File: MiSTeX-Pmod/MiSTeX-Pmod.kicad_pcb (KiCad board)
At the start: 4 copper layers, 64.2 x 51.3 mm, 30 parts, among them CN1 NASB0-S6701-TS50, CN2 NASB0-S6701-TS50, J1 Pmod, J2 USB_A, J3 Conn_01x03_Male, J4 Pmod, J5 Connector_USB_C_Receptacle_US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, SW1 TS-1187A-B-A-B

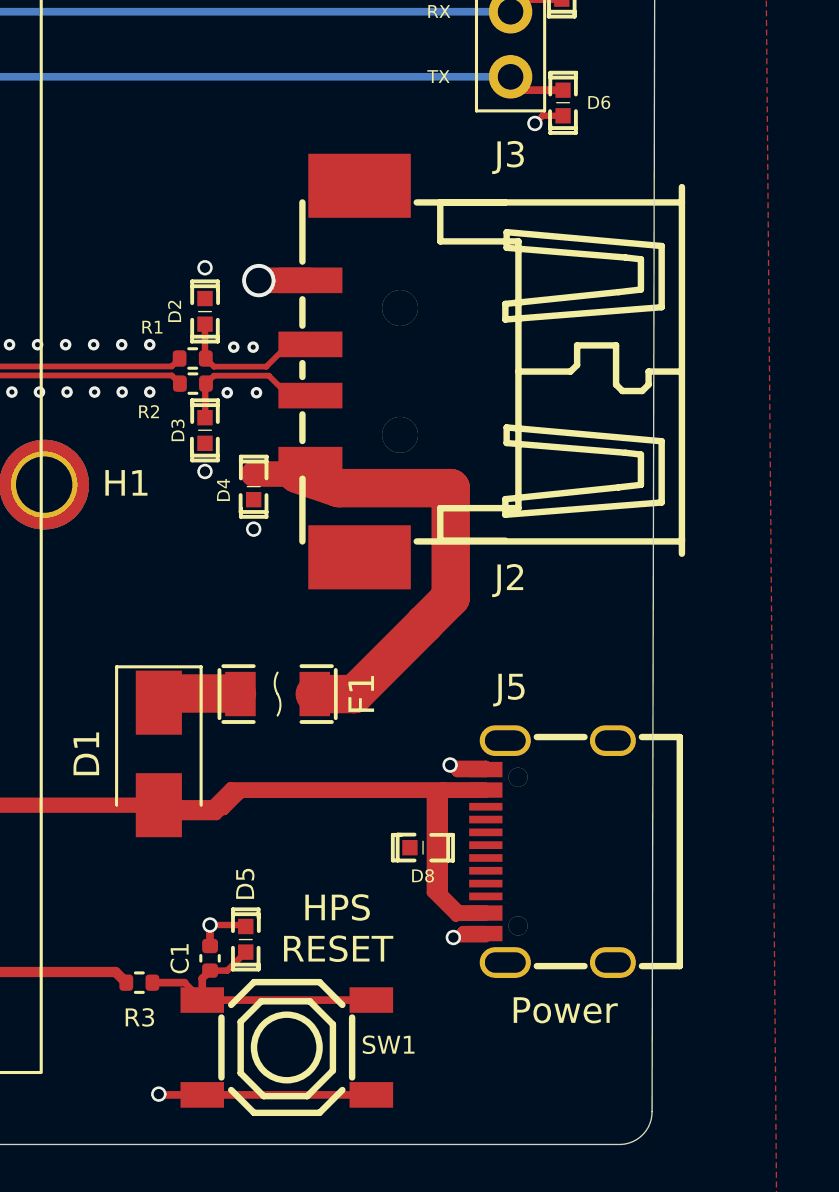
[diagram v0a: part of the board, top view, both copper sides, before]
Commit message: change USB host connector, old one was out of stock
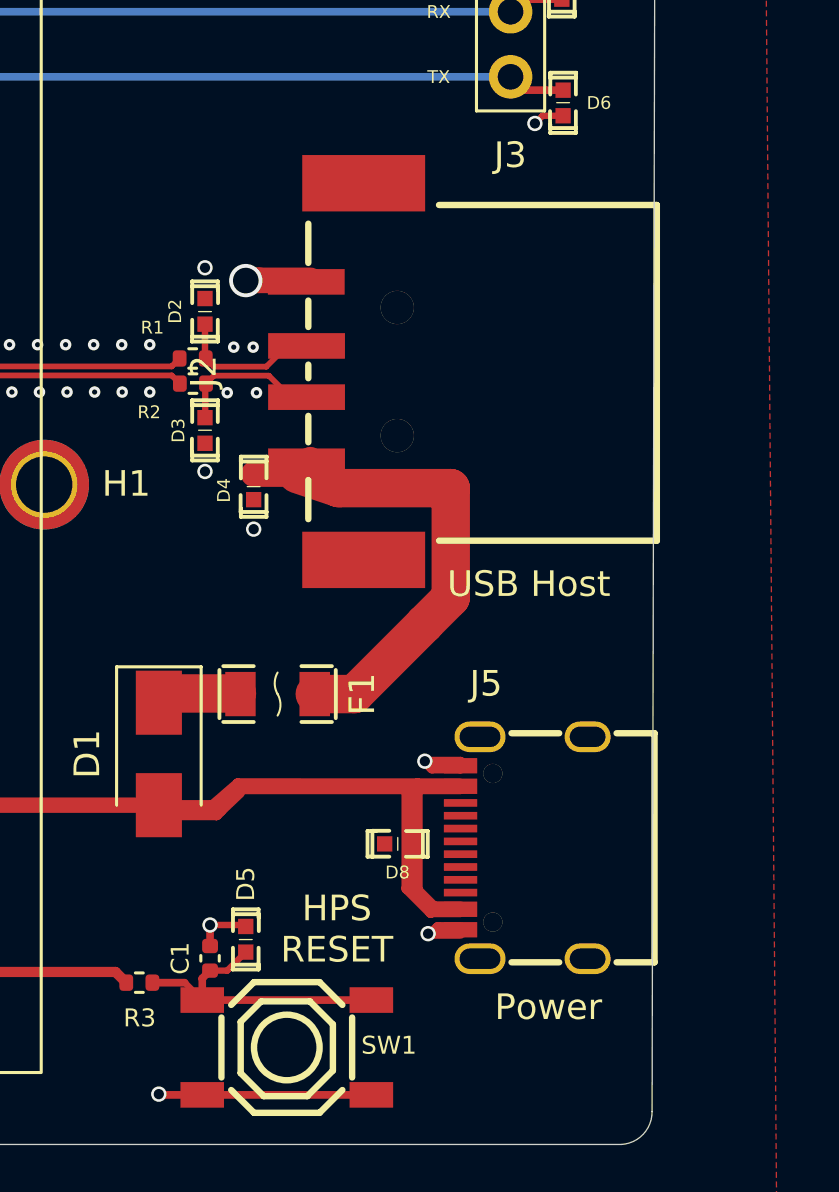
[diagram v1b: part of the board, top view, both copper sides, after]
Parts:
- J2: footprint easyeda2kicad:USB-A-SMD_USB-302S -> easyeda2kicad:USB-A-SMD_GT-USB-2004-CWG1A
- moved D8 1.00 mm to (168.6, 110.3)
- moved J5 1.00 mm to (173.5, 110.5)
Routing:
- net +5V: track 75.7 -> 73.8 mm
- net GND: track 71.4 -> 71.9 mm
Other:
- board text added: "USB Host"

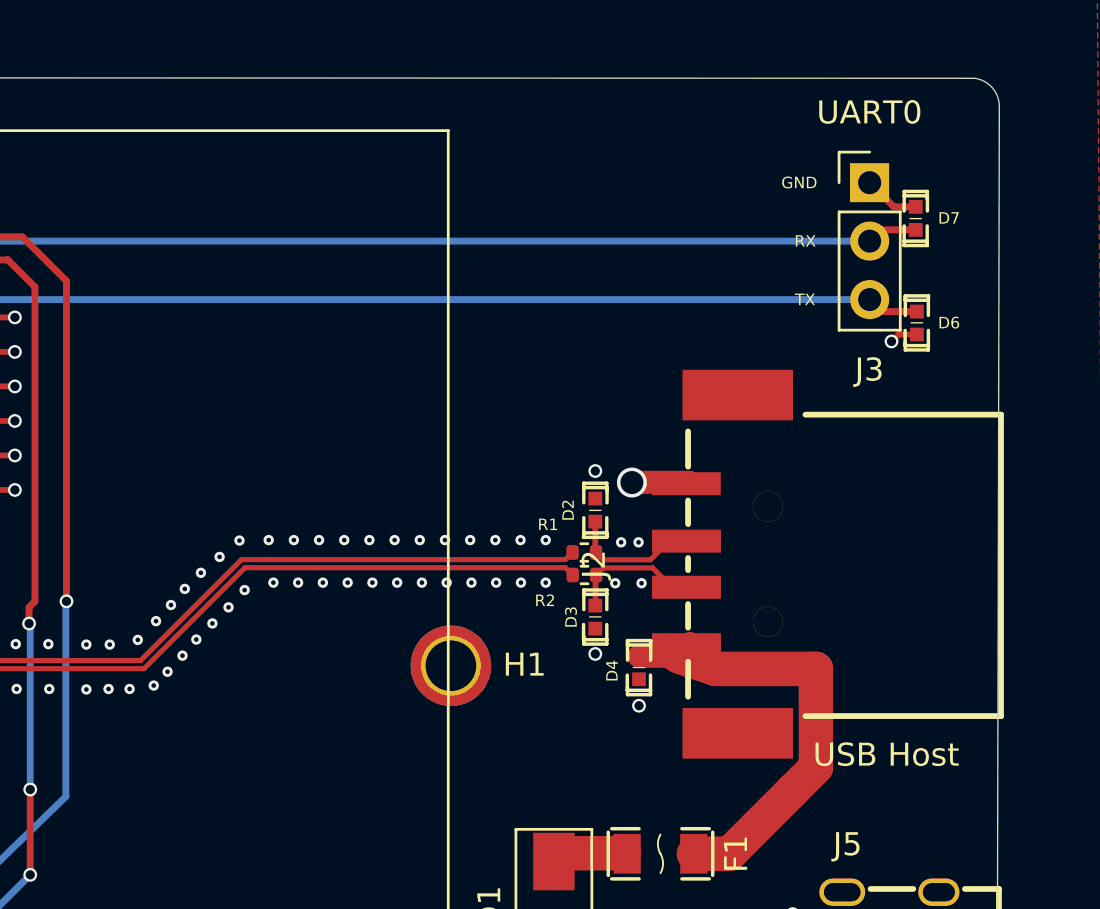
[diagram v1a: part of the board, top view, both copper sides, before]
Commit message: MiSTeX Pmod: fix USB emc protection diode stubs
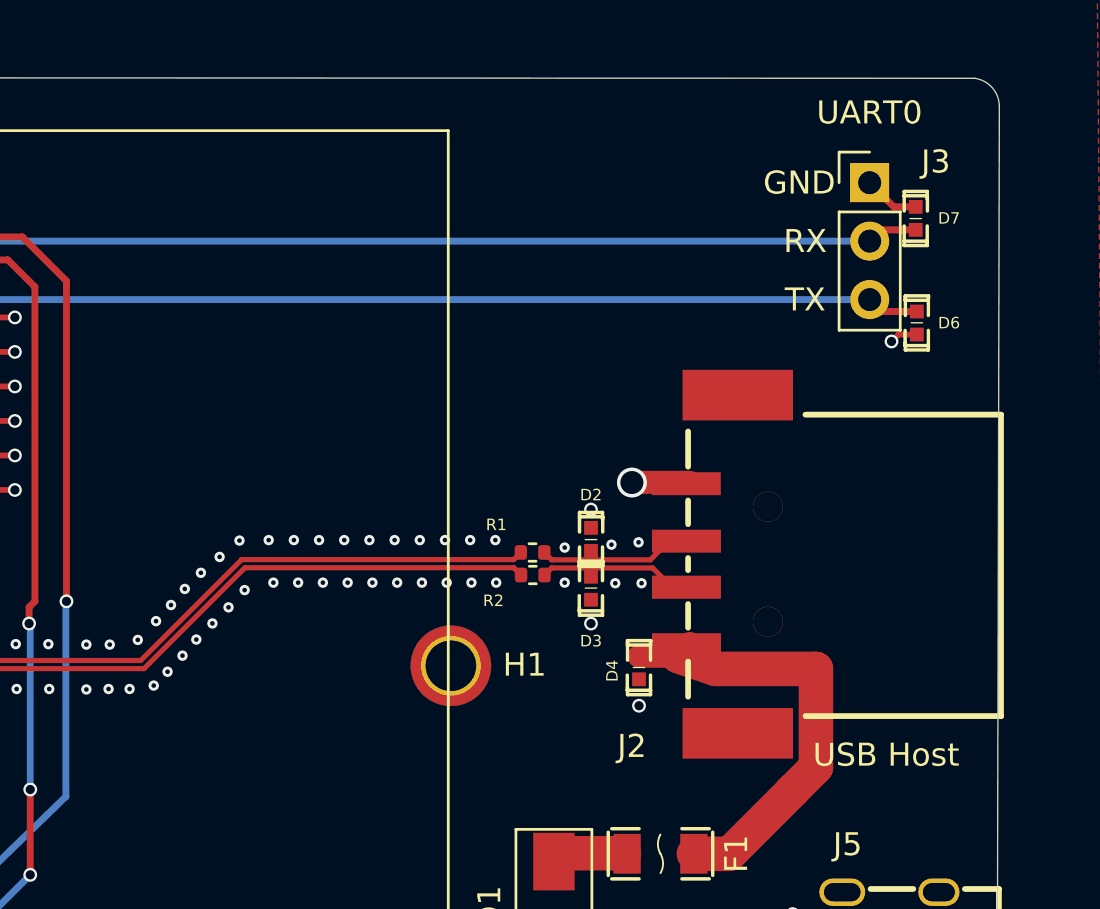
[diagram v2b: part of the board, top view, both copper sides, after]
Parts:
- moved R2 2.25 mm to (158.4, 92.4)
- moved R1 2.25 mm to (158.4, 91.4)
- moved D2 1.28 mm to (160.9, 90.8)
- moved D3 1.27 mm to (160.9, 93.0)
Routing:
- net /USB_HOST_P: track 52.8 -> 50.5 mm
- net /USB_HOST_N: track 51.6 -> 49.4 mm
- net /D+: track 6.59 -> 7.58 mm
- net /D-: track 8.28 -> 9.14 mm
- net GND: vias 124 -> 122
